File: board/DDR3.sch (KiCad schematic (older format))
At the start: 56 parts, among them U1 MT41J128M16

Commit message: Importing footprint names into schematic.
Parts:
- C1, C10, C11, C12, C13, C14, C15, C16, C17, C174, C176, C178, C18, C180, C182, C184, C186, C187, C19, C2, C20, C207, C209, C21, C22, C23, C24, C25, C26, C27, C28, C29, C3, C30, C31, C32, C33, C4, C5, C6, C7, C8, C9, R11, R12, R4, R5, R6, R7: footprint (none) -> SM0402
- R1: footprint (none) -> SM0603
- R10, R2, R3, R8, R9: footprint ~ -> RES_NET4
- U1: footprint ~ -> BGA96-0.8

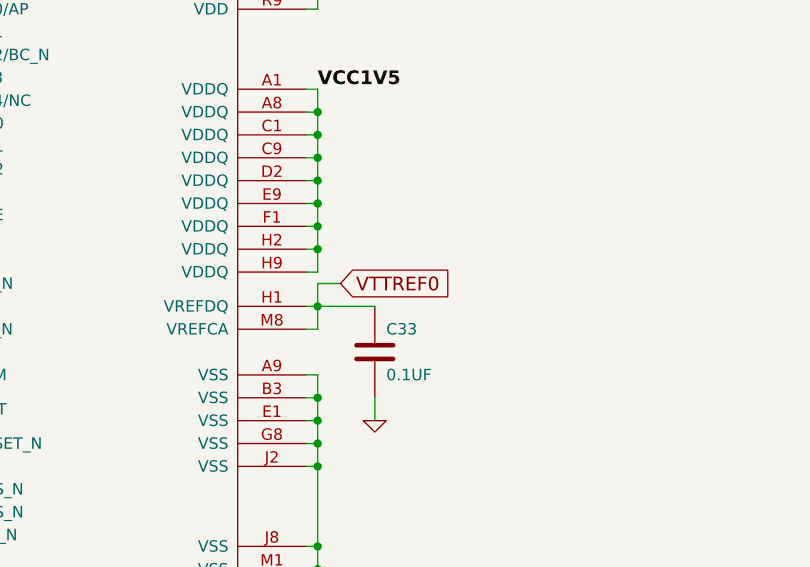
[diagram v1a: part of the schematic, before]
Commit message: s/VTTREF0/VTTREF/
https://github.com/timvideos/HDMI2USB-numato-opsis-hardware/issues/12
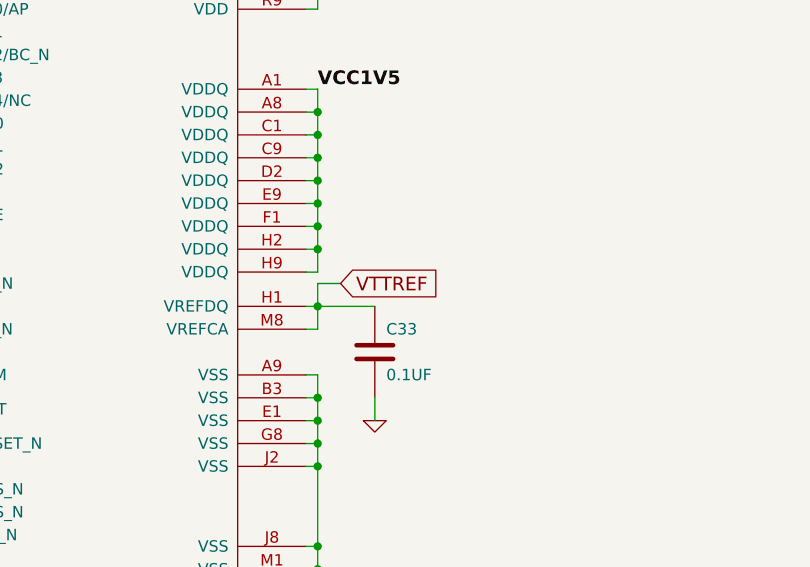
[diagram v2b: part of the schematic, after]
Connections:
- net VTTREF0 renamed VTTREF
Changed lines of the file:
@@
 Sheet 5 12
 Title "HDMI2USB"
-Date "23 jul 2015"
+Date "25 aug 2015"
 Rev "Rev2"
 Comp ""
@@
 VTTDDR0
 Text GLabel 11950 3500 2    60   Input ~ 0
-VTTREF0
+VTTREF
 Wire Wire Line
 	11800 5500 11850 5500

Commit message: s/UF/uF/gc
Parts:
- C1, C10, C11, C12, C13, C14, C15, C16, C17, C174, C176, C178, C18, C180, C182, C184, C186, C187, C19, C2, C20, C207, C209, C21, C22, C23, C24, C25, C26, C27, C28, C29, C3, C30, C31, C32, C33, C4, C5, C6, C7, C8, C9: value 0.1UF -> 0.1uF
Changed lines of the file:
@@
 P 12100 3800
 F 0 "C33" H 12150 3900 50  0000 L CNN
-F 1 "0.1UF" H 12150 3700 50  0000 L CNN
+F 1 "0.1uF" H 12150 3700 50  0000 L CNN
 F 2 "SM0402" H 12100 3800 60  0001 C CNN
 F 3 "" H 12100 3800 60  0000 C CNN
@@
 P 2200 8800
 F 0 "C1" H 2250 8900 50  0000 L CNN
-F 1 "0.1UF" H 2250 8700 50  0000 L CNN
+F 1 "0.1uF" H 2250 8700 50  0000 L CNN
 F 2 "SM0402" H 2200 8800 60  0001 C CNN
 F 3 "" H 2200 8800 60  0000 C CNN
@@
 P 2550 8800
 F 0 "C2" H 2600 8900 50  0000 L CNN
-F 1 "0.1UF" H 2600 8700 50  0000 L CNN
+F 1 "0.1uF" H 2600 8700 50  0000 L CNN
 F 2 "SM0402" H 2550 8800 60  0001 C CNN
 F 3 "" H 2550 8800 60  0000 C CNN
@@
 P 2950 8800
 F 0 "C3" H 3000 8900 50  0000 L CNN
-F 1 "0.1UF" H 3000 8700 50  0000 L CNN
+F 1 "0.1uF" H 3000 8700 50  0000 L CNN
 F 2 "SM0402" H 2950 8800 60  0001 C CNN
 F 3 "" H 2950 8800 60  0000 C CNN
@@
 P 3350 8800
 F 0 "C4" H 3400 8900 50  0000 L CNN
-F 1 "0.1UF" H 3400 8700 50  0000 L CNN
+F 1 "0.1uF" H 3400 8700 50  0000 L CNN
 F 2 "SM0402" H 3350 8800 60  0001 C CNN
 F 3 "" H 3350 8800 60  0000 C CNN
@@
 P 3700 8800
 F 0 "C5" H 3750 8900 50  0000 L CNN
-F 1 "0.1UF" H 3750 8700 50  0000 L CNN
+F 1 "0.1uF" H 3750 8700 50  0000 L CNN
 F 2 "SM0402" H 3700 8800 60  0001 C CNN
 F 3 "" H 3700 8800 60  0000 C CNN
@@
 P 4050 8800
 F 0 "C6" H 4100 8900 50  0000 L CNN
-F 1 "0.1UF" H 4100 8700 50  0000 L CNN
+F 1 "0.1uF" H 4100 8700 50  0000 L CNN
 F 2 "SM0402" H 4050 8800 60  0001 C CNN
 F 3 "" H 4050 8800 60  0000 C CNN
@@
 P 4500 8800
 F 0 "C7" H 4550 8900 50  0000 L CNN
-F 1 "0.1UF" H 4550 8700 50  0000 L CNN
+F 1 "0.1uF" H 4550 8700 50  0000 L CNN
 F 2 "SM0402" H 4500 8800 60  0001 C CNN
 F 3 "" H 4500 8800 60  0000 C CNN
@@
 P 4900 8800
 F 0 "C8" H 4950 8900 50  0000 L CNN
-F 1 "0.1UF" H 4950 8700 50  0000 L CNN
+F 1 "0.1uF" H 4950 8700 50  0000 L CNN
 F 2 "SM0402" H 4900 8800 60  0001 C CNN
 F 3 "" H 4900 8800 60  0000 C CNN
@@
 P 5300 8800
 F 0 "C9" H 5350 8900 50  0000 L CNN
-F 1 "0.1UF" H 5350 8700 50  0000 L CNN
+F 1 "0.1uF" H 5350 8700 50  0000 L CNN
 F 2 "SM0402" H 5300 8800 60  0001 C CNN
 F 3 "" H 5300 8800 60  0000 C CNN
@@
 P 5650 8800
 F 0 "C10" H 5700 8900 50  0000 L CNN
-F 1 "0.1UF" H 5700 8700 50  0000 L CNN
+F 1 "0.1uF" H 5700 8700 50  0000 L CNN
 F 2 "SM0402" H 5650 8800 60  0001 C CNN
 F 3 "" H 5650 8800 60  0000 C CNN
@@
 P 6100 8800
 F 0 "C11" H 6150 8900 50  0000 L CNN
-F 1 "0.1UF" H 6150 8700 50  0000 L CNN
+F 1 "0.1uF" H 6150 8700 50  0000 L CNN
 F 2 "SM0402" H 6100 8800 60  0001 C CNN
 F 3 "" H 6100 8800 60  0000 C CNN
@@
 P 6550 8800
 F 0 "C12" H 6600 8900 50  0000 L CNN
-F 1 "0.1UF" H 6600 8700 50  0000 L CNN
+F 1 "0.1uF" H 6600 8700 50  0000 L CNN
 F 2 "SM0402" H 6550 8800 60  0001 C CNN
 F 3 "" H 6550 8800 60  0000 C CNN
@@
 P 6950 8800
 F 0 "C13" H 7000 8900 50  0000 L CNN
-F 1 "0.1UF" H 7000 8700 50  0000 L CNN
+F 1 "0.1uF" H 7000 8700 50  0000 L CNN
 F 2 "SM0402" H 6950 8800 60  0001 C CNN
 F 3 "" H 6950 8800 60  0000 C CNN
@@
 P 7350 8800
 F 0 "C14" H 7400 8900 50  0000 L CNN
-F 1 "0.1UF" H 7400 8700 50  0000 L CNN
+F 1 "0.1uF" H 7400 8700 50  0000 L CNN
 F 2 "SM0402" H 7350 8800 60  0001 C CNN
 F 3 "" H 7350 8800 60  0000 C CNN
@@
 P 7750 8800
 F 0 "C15" H 7800 8900 50  0000 L CNN
-F 1 "0.1UF" H 7800 8700 50  0000 L CNN
+F 1 "0.1uF" H 7800 8700 50  0000 L CNN
 F 2 "SM0402" H 7750 8800 60  0001 C CNN
 F 3 "" H 7750 8800 60  0000 C CNN
@@
 P 2200 8300
 F 0 "C16" H 2250 8400 50  0000 L CNN
-F 1 "0.1UF" H 2250 8200 50  0000 L CNN
+F 1 "0.1uF" H 2250 8200 50  0000 L CNN
 F 2 "SM0402" H 2200 8300 60  0001 C CNN
 F 3 "" H 2200 8300 60  0000 C CNN
@@
 P 2550 8300
 F 0 "C17" H 2600 8400 50  0000 L CNN
-F 1 "0.1UF" H 2600 8200 50  0000 L CNN
+F 1 "0.1uF" H 2600 8200 50  0000 L CNN
 F 2 "SM0402" H 2550 8300 60  0001 C CNN
 F 3 "" H 2550 8300 60  0000 C CNN
@@
 P 2950 8300
 F 0 "C18" H 3000 8400 50  0000 L CNN
-F 1 "0.1UF" H 3000 8200 50  0000 L CNN
+F 1 "0.1uF" H 3000 8200 50  0000 L CNN
 F 2 "SM0402" H 2950 8300 60  0001 C CNN
 F 3 "" H 2950 8300 60  0000 C CNN
@@
 P 3350 8250
 F 0 "C19" H 3400 8350 50  0000 L CNN
-F 1 "0.1UF" H 3400 8150 50  0000 L CNN
+F 1 "0.1uF" H 3400 8150 50  0000 L CNN
 F 2 "SM0402" H 3350 8250 60  0001 C CNN
 F 3 "" H 3350 8250 60  0000 C CNN
@@
 P 3700 8250
 F 0 "C20" H 3750 8350 50  0000 L CNN
-F 1 "0.1UF" H 3750 8150 50  0000 L CNN
+F 1 "0.1uF" H 3750 8150 50  0000 L CNN
 F 2 "SM0402" H 3700 8250 60  0001 C CNN
 F 3 "" H 3700 8250 60  0000 C CNN
@@
 P 4050 8250
 F 0 "C21" H 4100 8350 50  0000 L CNN
-F 1 "0.1UF" H 4100 8150 50  0000 L CNN
+F 1 "0.1uF" H 4100 8150 50  0000 L CNN
 F 2 "SM0402" H 4050 8250 60  0001 C CNN
 F 3 "" H 4050 8250 60  0000 C CNN
@@
 P 4500 8250
 F 0 "C22" H 4550 8350 50  0000 L CNN
-F 1 "0.1UF" H 4550 8150 50  0000 L CNN
+F 1 "0.1uF" H 4550 8150 50  0000 L CNN
 F 2 "SM0402" H 4500 8250 60  0001 C CNN
 F 3 "" H 4500 8250 60  0000 C CNN
@@
 P 4900 8250
 F 0 "C23" H 4950 8350 50  0000 L CNN
-F 1 "0.1UF" H 4950 8150 50  0000 L CNN
+F 1 "0.1uF" H 4950 8150 50  0000 L CNN
 F 2 "SM0402" H 4900 8250 60  0001 C CNN
 F 3 "" H 4900 8250 60  0000 C CNN
@@
 P 5300 8250
 F 0 "C24" H 5350 8350 50  0000 L CNN
-F 1 "0.1UF" H 5350 8150 50  0000 L CNN
+F 1 "0.1uF" H 5350 8150 50  0000 L CNN
 F 2 "SM0402" H 5300 8250 60  0001 C CNN
 F 3 "" H 5300 8250 60  0000 C CNN
@@
 P 5650 8250
 F 0 "C25" H 5700 8350 50  0000 L CNN
-F 1 "0.1UF" H 5700 8150 50  0000 L CNN
+F 1 "0.1uF" H 5700 8150 50  0000 L CNN
 F 2 "SM0402" H 5650 8250 60  0001 C CNN
 F 3 "" H 5650 8250 60  0000 C CNN
@@
 P 6100 8250
 F 0 "C26" H 6150 8350 50  0000 L CNN
-F 1 "0.1UF" H 6150 8150 50  0000 L CNN
+F 1 "0.1uF" H 6150 8150 50  0000 L CNN
 F 2 "SM0402" H 6100 8250 60  0001 C CNN
 F 3 "" H 6100 8250 60  0000 C CNN
@@
 P 6550 8250
 F 0 "C27" H 6600 8350 50  0000 L CNN
-F 1 "0.1UF" H 6600 8150 50  0000 L CNN
+F 1 "0.1uF" H 6600 8150 50  0000 L CNN
 F 2 "SM0402" H 6550 8250 60  0001 C CNN
 F 3 "" H 6550 8250 60  0000 C CNN
@@
 P 6950 8250
 F 0 "C28" H 7000 8350 50  0000 L CNN
-F 1 "0.1UF" H 7000 8150 50  0000 L CNN
+F 1 "0.1uF" H 7000 8150 50  0000 L CNN
 F 2 "SM0402" H 6950 8250 60  0001 C CNN
 F 3 "" H 6950 8250 60  0000 C CNN
@@
 P 7350 8250
 F 0 "C29" H 7400 8350 50  0000 L CNN
-F 1 "0.1UF" H 7400 8150 50  0000 L CNN
+F 1 "0.1uF" H 7400 8150 50  0000 L CNN
 F 2 "SM0402" H 7350 8250 60  0001 C CNN
 F 3 "" H 7350 8250 60  0000 C CNN
@@
 P 7750 8250
 F 0 "C30" H 7800 8350 50  0000 L CNN
-F 1 "0.1UF" H 7800 8150 50  0000 L CNN
+F 1 "0.1uF" H 7800 8150 50  0000 L CNN
 F 2 "SM0402" H 7750 8250 60  0001 C CNN
 F 3 "" H 7750 8250 60  0000 C CNN
@@
 P 8050 8250
 F 0 "C31" H 8100 8350 50  0000 L CNN
-F 1 "0.1UF" H 8100 8150 50  0000 L CNN
+F 1 "0.1uF" H 8100 8150 50  0000 L CNN
 F 2 "SM0402" H 8050 8250 60  0001 C CNN
 F 3 "" H 8050 8250 60  0000 C CNN
@@
 P 8350 8250
 F 0 "C32" H 8400 8350 50  0000 L CNN
-F 1 "0.1UF" H 8400 8150 50  0000 L CNN
+F 1 "0.1uF" H 8400 8150 50  0000 L CNN
 F 2 "SM0402" H 8350 8250 60  0001 C CNN
 F 3 "" H 8350 8250 60  0000 C CNN
@@
 P 2000 9750
 F 0 "C174" H 2050 9850 50  0000 L CNN
-F 1 "0.1UF" H 2050 9650 50  0000 L CNN
+F 1 "0.1uF" H 2050 9650 50  0000 L CNN
 F 2 "SM0402" H 2000 9750 60  0001 C CNN
 F 3 "" H 2000 9750 60  0000 C CNN
@@
 P 2300 9750
 F 0 "C176" H 2350 9850 50  0000 L CNN
-F 1 "0.1UF" H 2350 9650 50  0000 L CNN
+F 1 "0.1uF" H 2350 9650 50  0000 L CNN
 F 2 "SM0402" H 2300 9750 60  0001 C CNN
 F 3 "" H 2300 9750 60  0000 C CNN
@@
 P 2600 9750
 F 0 "C178" H 2650 9850 50  0000 L CNN
-F 1 "0.1UF" H 2650 9650 50  0000 L CNN
+F 1 "0.1uF" H 2650 9650 50  0000 L CNN
 F 2 "SM0402" H 2600 9750 60  0001 C CNN
 F 3 "" H 2600 9750 60  0000 C CNN
@@
 P 2900 9750
 F 0 "C180" H 2950 9850 50  0000 L CNN
-F 1 "0.1UF" H 2950 9650 50  0000 L CNN
+F 1 "0.1uF" H 2950 9650 50  0000 L CNN
 F 2 "SM0402" H 2900 9750 60  0001 C CNN
 F 3 "" H 2900 9750 60  0000 C CNN
@@
 P 3200 9750
 F 0 "C182" H 3250 9850 50  0000 L CNN
-F 1 "0.1UF" H 3250 9650 50  0000 L CNN
+F 1 "0.1uF" H 3250 9650 50  0000 L CNN
 F 2 "SM0402" H 3200 9750 60  0001 C CNN
 F 3 "" H 3200 9750 60  0000 C CNN
@@
 P 3500 9750
 F 0 "C184" H 3550 9850 50  0000 L CNN
-F 1 "0.1UF" H 3550 9650 50  0000 L CNN
+F 1 "0.1uF" H 3550 9650 50  0000 L CNN
 F 2 "SM0402" H 3500 9750 60  0001 C CNN
 F 3 "" H 3500 9750 60  0000 C CNN
@@
 P 3800 9750
 F 0 "C186" H 3850 9850 50  0000 L CNN
-F 1 "0.1UF" H 3850 9650 50  0000 L CNN
+F 1 "0.1uF" H 3850 9650 50  0000 L CNN
 F 2 "SM0402" H 3800 9750 60  0001 C CNN
 F 3 "" H 3800 9750 60  0000 C CNN
@@
 P 4150 9750
 F 0 "C187" H 4200 9850 50  0000 L CNN
-F 1 "0.1UF" H 4200 9650 50  0000 L CNN
+F 1 "0.1uF" H 4200 9650 50  0000 L CNN
 F 2 "SM0402" H 4150 9750 60  0001 C CNN
 F 3 "" H 4150 9750 60  0000 C CNN
@@
 P 4450 9750
 F 0 "C207" H 4500 9850 50  0000 L CNN
-F 1 "0.1UF" H 4500 9650 50  0000 L CNN
+F 1 "0.1uF" H 4500 9650 50  0000 L CNN
 F 2 "SM0402" H 4450 9750 60  0001 C CNN
 F 3 "" H 4450 9750 60  0000 C CNN
@@
 P 4750 9750
 F 0 "C209" H 4800 9850 50  0000 L CNN
-F 1 "0.1UF" H 4800 9650 50  0000 L CNN
+F 1 "0.1uF" H 4800 9650 50  0000 L CNN
 F 2 "SM0402" H 4750 9750 60  0001 C CNN
 F 3 "" H 4750 9750 60  0000 C CNN
